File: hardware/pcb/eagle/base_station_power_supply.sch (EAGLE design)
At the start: 17 parts, among them CON1 POWER_JACKPTH, IC1 MB16S-TP

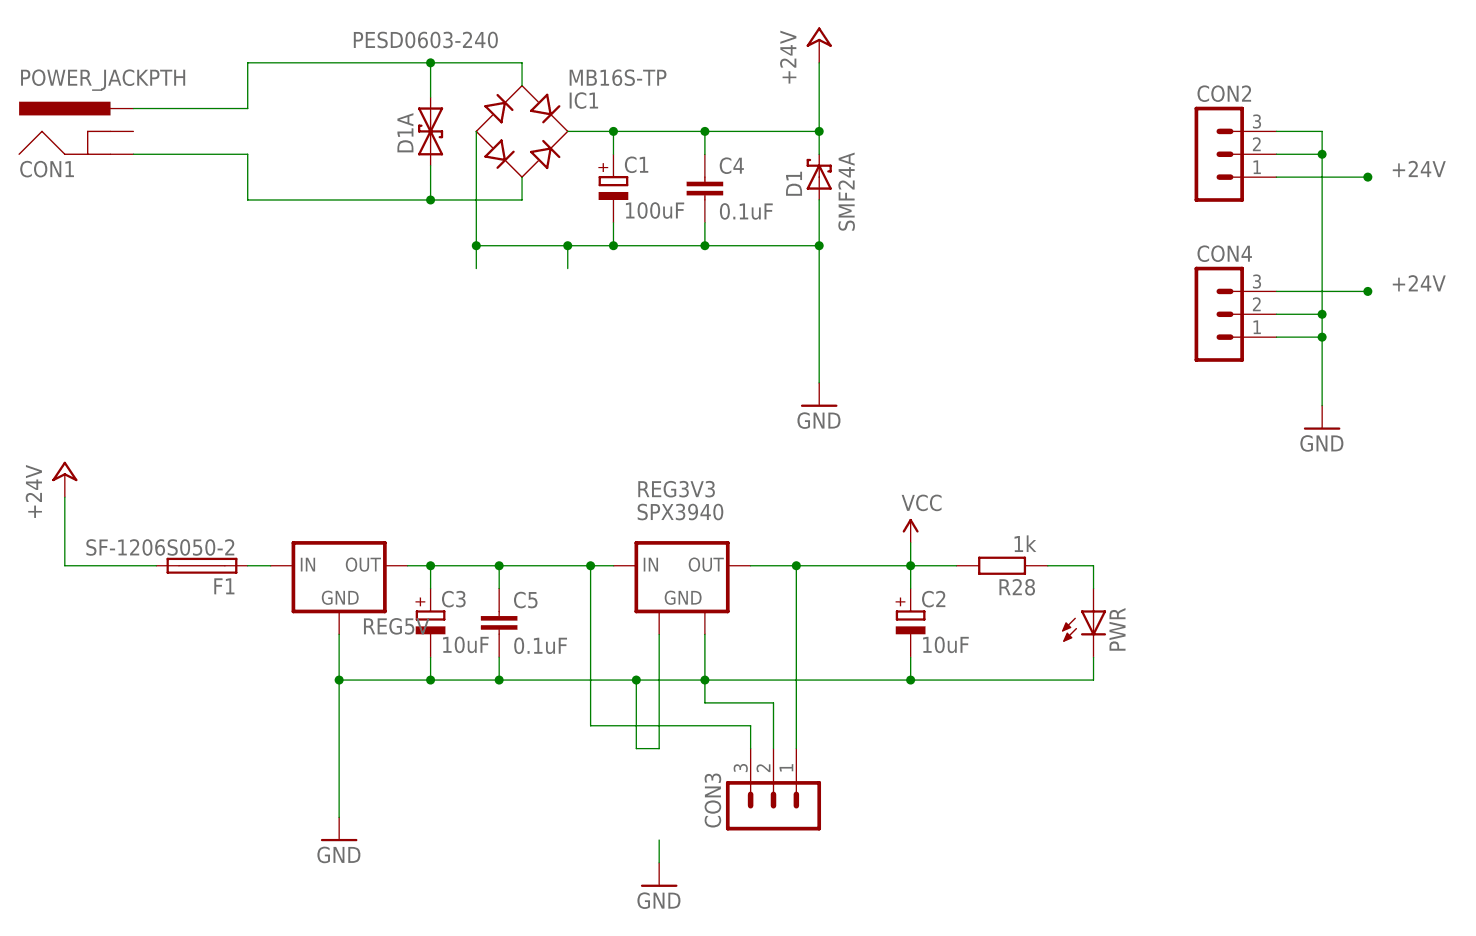
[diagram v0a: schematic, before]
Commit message: Silk screen layer tidied up
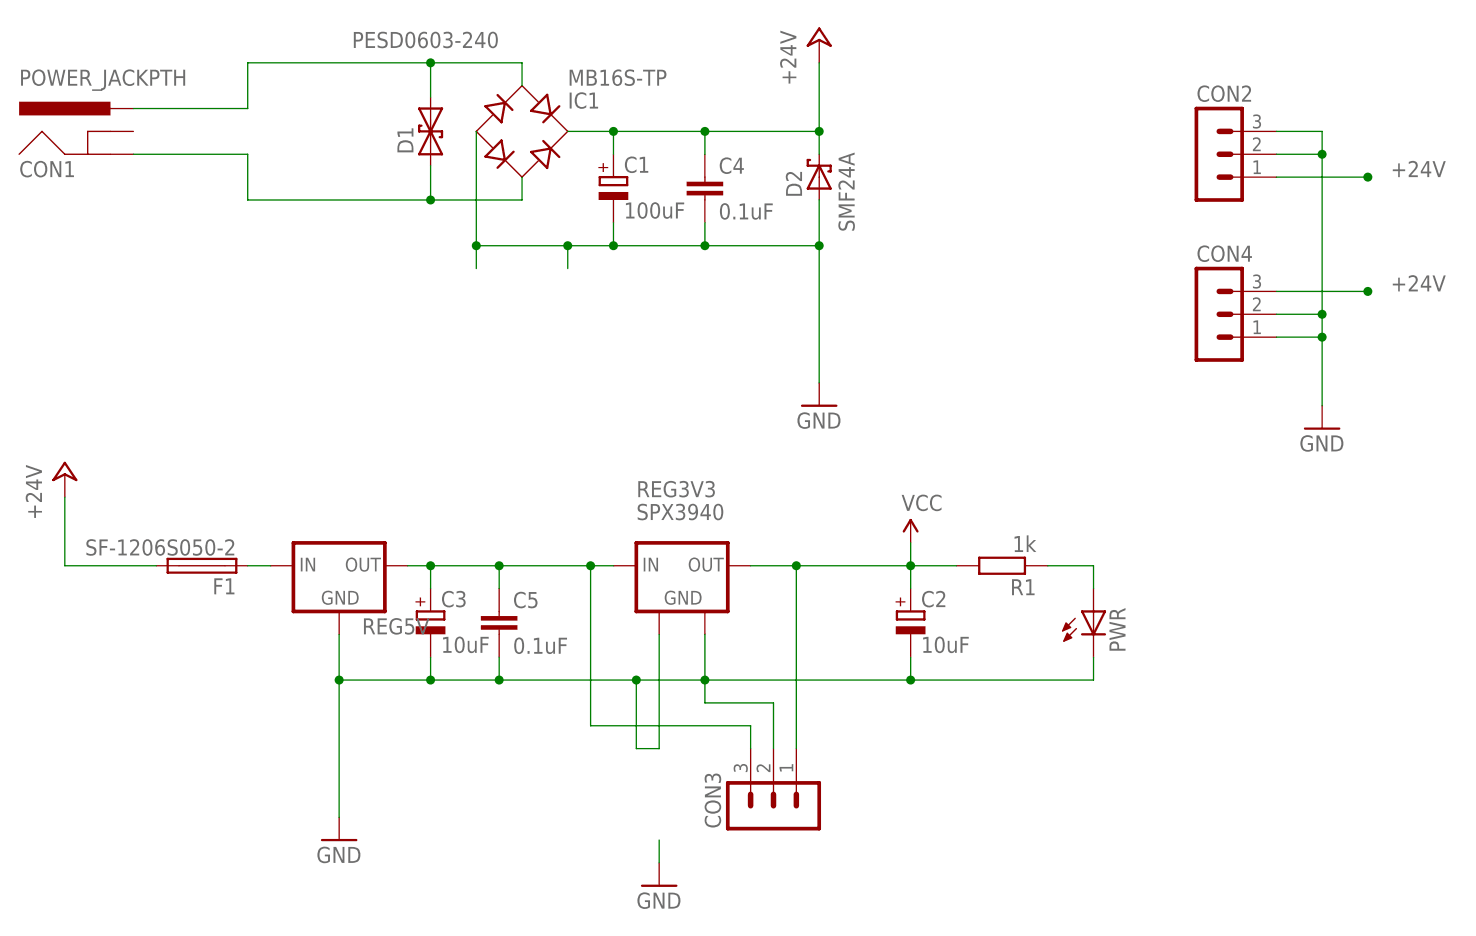
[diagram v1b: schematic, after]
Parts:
- removed D1A: PESD0603-240, texas_lvds:PESD0603-240
- added D2: SMF24A, texas_lvds:SMF24A
- D1: value SMF24A -> PESD0603-240; device texas_lvds:SMF24A -> texas_lvds:PESD0603-240
- renumbered R28 to R1
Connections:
- net +24V: now also D2.C; no longer D1.C
- net GNDINT: now also D2.A; no longer D1.A
- net N$7: now also D1.2; no longer D1A.2
- net N$8: now also D1.1; no longer D1A.1
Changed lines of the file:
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@@
 <part name="CON1" library="SparkFun" deviceset="POWER_JACK" device="PTH"/>
 <part name="IC1" library="texas_lvds" deviceset="MB16S-TP" device=""/>
-<part name="D1" library="texas_lvds" deviceset="SMF24A" device=""/>
-<part name="D1A" library="texas_lvds" deviceset="PESD0603-240" device=""/>
+<part name="D2" library="texas_lvds" deviceset="SMF24A" device=""/>
+<part name="D1" library="texas_lvds" deviceset="PESD0603-240" device=""/>
 <part name="C4" library="rcl" deviceset="C-EU" device="C0805" value="0.1uF"/>
 <part name="PWR" library="led" deviceset="LED" device="CHIPLED_0805"/>
-<part name="R28" library="rcl" deviceset="R-EU_" device="R0603" value="1k"/>
+<part name="R1" library="rcl" deviceset="R-EU_" device="R0603" value="1k"/>
 <part name="C1" library="rcl" deviceset="CPOL-EU" device="E5-10.5" value="100uF"/>
 <part name="C3" library="rcl" deviceset="CPOL-EU" device="E5-10.5" value="10uF"/>
@@
 <attribute name="NAME" x="347.98" y="304.8" size="1.778" layer="95"/>
 </instance>
-<instance part="D1" gate="1" x="375.92" y="297.18" smashed="yes" rot="R90">
+<instance part="D2" gate="1" x="375.92" y="297.18" smashed="yes" rot="R90">
 <attribute name="NAME" x="374.015" y="294.894" size="1.778" layer="95" rot="R90"/>
 <attribute name="VALUE" x="379.857" y="291.084" size="1.778" layer="96" rot="R90"/>
 </instance>
-<instance part="D1A" gate="G$1" x="332.74" y="300.99" smashed="yes" rot="R90">
+<instance part="D1" gate="G$1" x="332.74" y="300.99" smashed="yes" rot="R90">
 <attribute name="NAME" x="330.835" y="299.72" size="1.778" layer="95" rot="R90"/>
 <attribute name="VALUE" x="340.36" y="313.309" size="1.778" layer="96" rot="R180"/>
@@
 <instance part="C4" gate="G$1" x="363.22" y="297.18"/>
 <instance part="PWR" gate="G$1" x="406.4" y="248.92"/>
-<instance part="R28" gate="G$1" x="396.24" y="254" rot="R180"/>
+<instance part="R1" gate="G$1" x="396.24" y="254" rot="R180"/>
 <instance part="C1" gate="G$1" x="353.06" y="297.18"/>
 <instance part="C3" gate="G$1" x="332.74" y="248.92"/>
@@
 <wire x1="386.08" y1="254" x2="386.08" y2="251.46" width="0.1524" layer="91"/>
 <junction x="386.08" y="254"/>
-<pinref part="R28" gate="G$1" pin="2"/>
+<pinref part="R1" gate="G$1" pin="2"/>
 <wire x1="391.16" y1="254" x2="386.08" y2="254" width="0.1524" layer="91"/>
 <pinref part="CON3" gate="G$1" pin="1"/>
@@
 <segment>
 <pinref part="IC1" gate="G$1" pin="+"/>
-<pinref part="D1" gate="1" pin="C"/>
+<pinref part="D2" gate="1" pin="C"/>
 <wire x1="375.92" y1="302.26" x2="363.22" y2="302.26" width="0.1524" layer="91"/>
 <wire x1="363.22" y1="302.26" x2="353.06" y2="302.26" width="0.1524" layer="91"/>
@@
 <wire x1="342.9" y1="309.88" x2="342.9" y2="307.34" width="0.1524" layer="91"/>
 <wire x1="332.74" y1="309.88" x2="342.9" y2="309.88" width="0.1524" layer="91"/>
-<pinref part="D1A" gate="G$1" pin="2"/>
+<pinref part="D1" gate="G$1" pin="2"/>
 <wire x1="332.74" y1="306.07" x2="332.74" y2="309.88" width="0.1524" layer="91"/>
 <junction x="332.74" y="309.88"/>
@@
 <wire x1="312.42" y1="299.72" x2="299.72" y2="299.72" width="0.1524" layer="91"/>
 <pinref part="CON1" gate="G$1" pin="GND"/>
-<pinref part="D1A" gate="G$1" pin="1"/>
+<pinref part="D1" gate="G$1" pin="1"/>
 <wire x1="332.74" y1="298.45" x2="332.74" y2="294.64" width="0.1524" layer="91"/>
 <junction x="332.74" y="294.64"/>
@@
 <net name="N$2" class="0">
 <segment>
-<pinref part="R28" gate="G$1" pin="1"/>
+<pinref part="R1" gate="G$1" pin="1"/>
 <pinref part="PWR" gate="G$1" pin="A"/>
 <wire x1="401.32" y1="254" x2="406.4" y2="254" width="0.1524" layer="91"/>
@@
 <segment>
 <pinref part="GND4" gate="1" pin="GND"/>
-<pinref part="D1" gate="1" pin="A"/>
+<pinref part="D2" gate="1" pin="A"/>
 <wire x1="375.92" y1="294.64" x2="375.92" y2="289.56" width="0.1524" layer="91"/>
 <junction x="375.92" y="289.56"/>
